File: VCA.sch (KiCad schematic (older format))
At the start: 27 parts, among them Q401 2N3904, Q402 2N3906, Q403 2N3904, U502 LM13700, U605 TL074

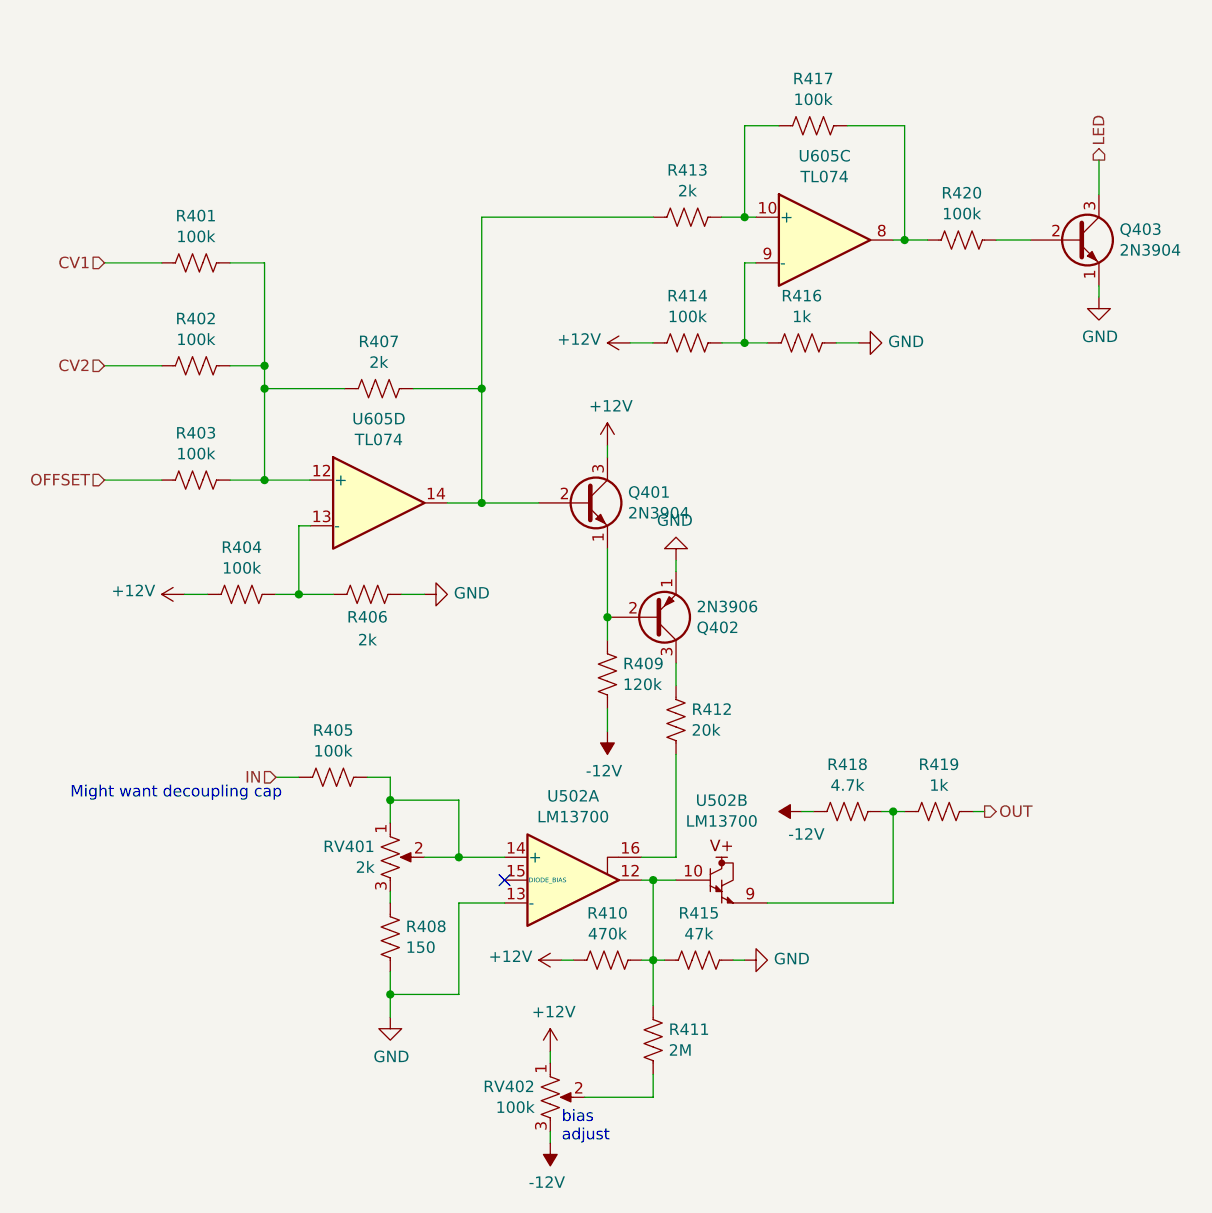
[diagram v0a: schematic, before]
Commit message: Began fixing backwards op amp issue
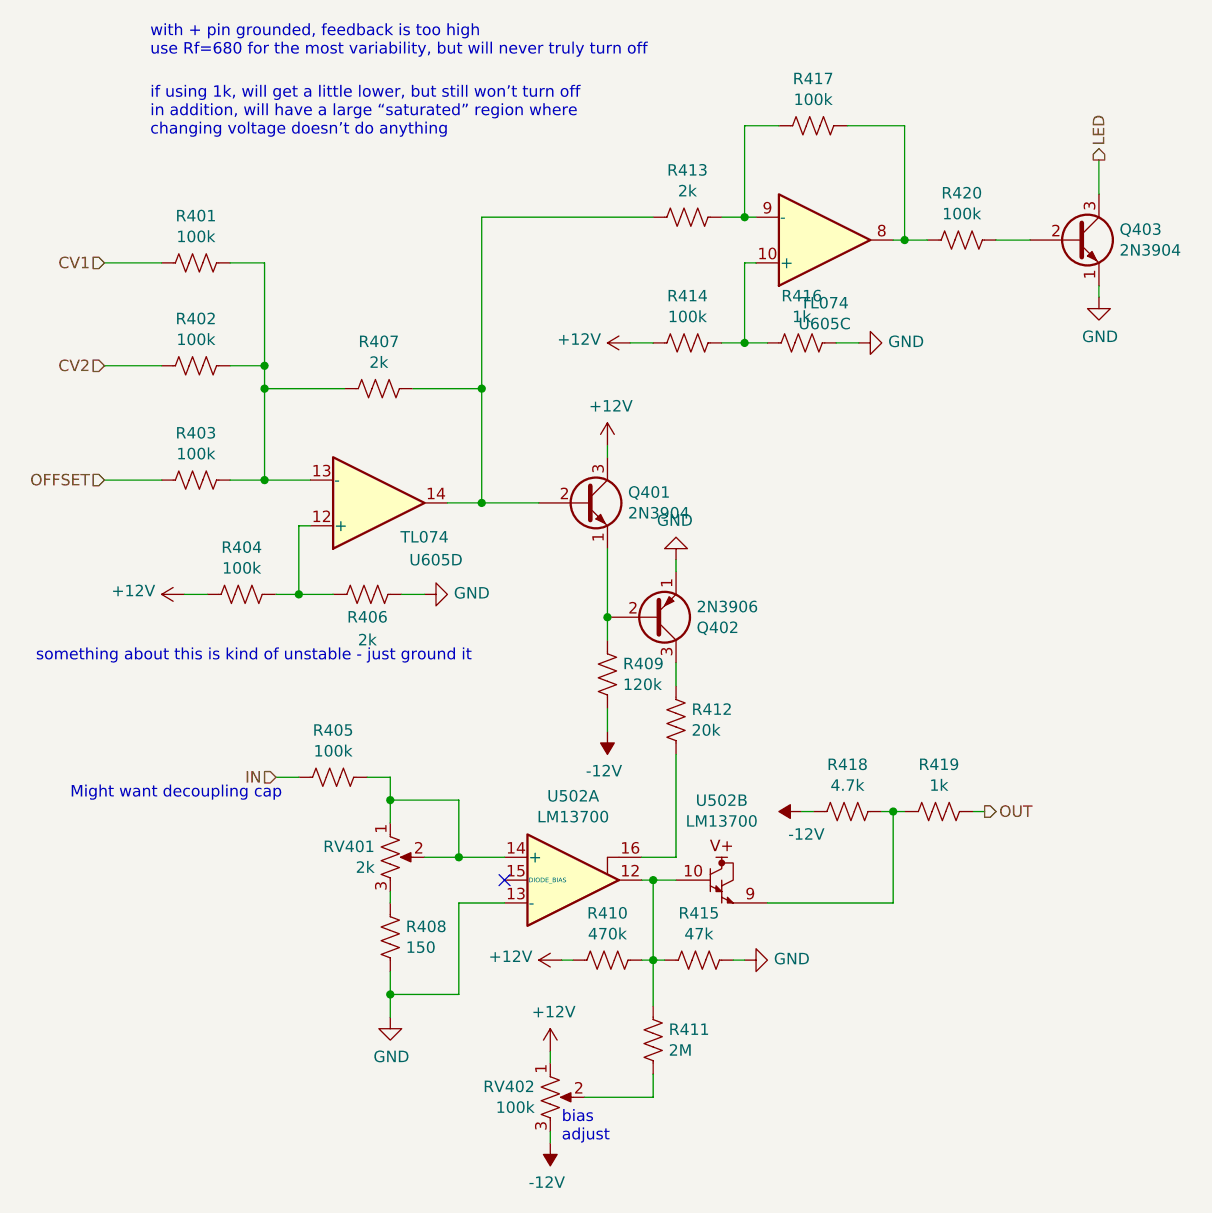
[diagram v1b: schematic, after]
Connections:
- net at R401.1, R402.1, R403.1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: now also U605.13 (-); no longer U605.12 (+)
- net at R404.1, R406.2: now also U605.12 (+); no longer U605.13 (-)
- net at R413.1, R417.2: now also U605.9 (-); no longer U605.10 (+)
- net at R414.1, R416.2: now also U605.10 (+); no longer U605.9 (-)
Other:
- note added: "if using 1k, will get a little lower, but still won’t turn off\nin addition, will have a large “saturated” region where \nchanging voltage doesn’t do anything"
- note added: "something about this is kind of unstable - just ground it"
- note added: "with + pin grounded, feedback is too high\nuse Rf=680 for the most variability, but will never truly turn off"
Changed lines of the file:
@@
 U 4 1 6035B5C1
 P 2400 3000
-F 0 "U605" H 2400 3367 50  0000 C CNN
-F 1 "TL074" H 2400 3276 50  0000 C CNN
+F 0 "U605" H 2650 3250 50  0000 C CNN
+F 1 "TL074" H 2600 3150 50  0000 C CNN
 F 2 "Package_DIP:DIP-14_W7.62mm" H 2400 3000 50  0001 C CNN
 F 3 "http://www.ti.com/lit/ds/symlink/tl081.pdf" H 2400 3000 50  0001 C CNN
 	4    2400 3000
-	1    0    0    -1
+	1    0    0    1
 $EndComp
 $Comp
@@
 F 3 "http://www.ti.com/lit/ds/symlink/tl081.pdf" H 4350 1850 50  0001 C CNN
 	3    4350 1850
-	1    0    0    -1
+	1    0    0    1
 $EndComp
 $Comp
@@
 Text Notes 3200 5800 0    50   ~ 0
 bias\nadjust
+Text Notes 900  3700 0    50   ~ 0
+something about this is kind of unstable - just ground it
+Text Notes 1400 1050 0    50   ~ 0
+with + pin grounded, feedback is too high\nuse Rf=680 for the most variability, but will never truly turn off
+Text Notes 1400 1400 0    50   ~ 0
+if using 1k, will get a little lower, but still won’t turn off\nin addition, will have a large “saturated” region where \nchanging voltage doesn’t do anything
 $EndSCHEMATC

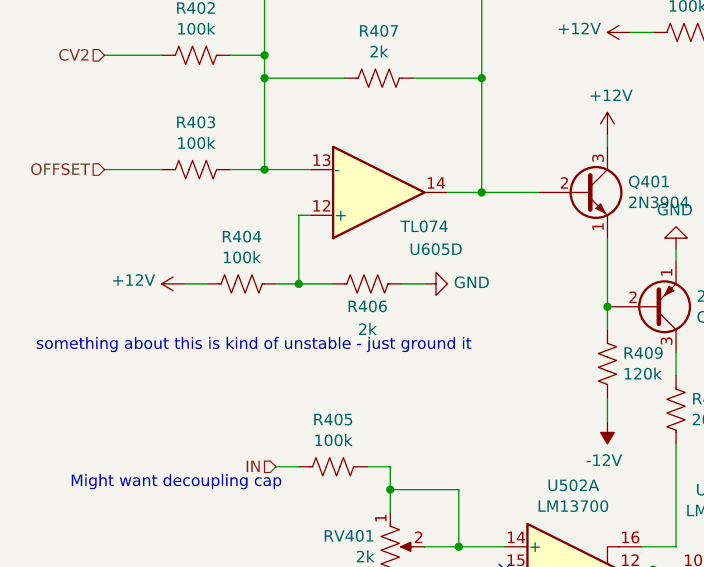
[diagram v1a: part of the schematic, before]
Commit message: Fixed op amp issue
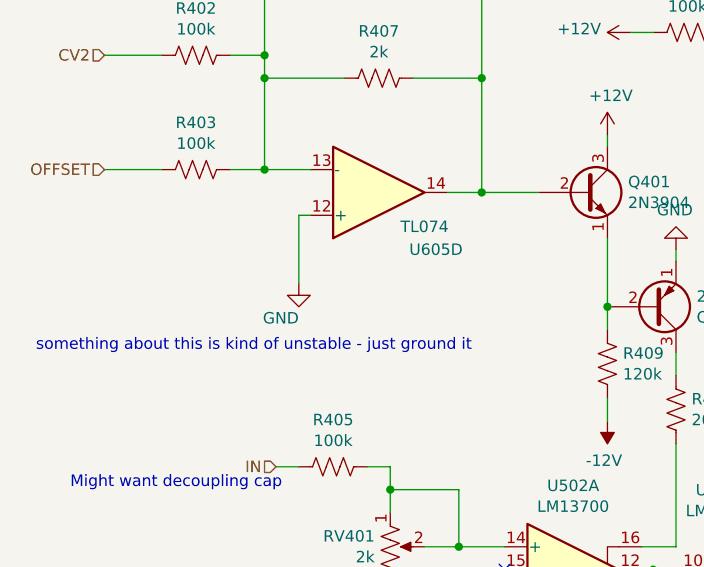
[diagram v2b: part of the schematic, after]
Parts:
- removed R404: 100k, Resistor_THT:R_Axial_DIN0207_L6.3mm_D2.5mm_P7.62mm_Horizontal, symbol Device:R_US
- removed R406: 2k, Resistor_THT:R_Axial_DIN0207_L6.3mm_D2.5mm_P7.62mm_Horizontal, symbol Device:R_US
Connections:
- net GND: now also U605.12 (+)
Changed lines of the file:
@@
-$EndComp
-$Comp
-L Device:R_US R406
-U 1 1 6036C3EB
-P 2350 3400
-F 0 "R406" V 2450 3400 50  0000 C CNN
-F 1 "2k" V 2550 3400 50  0000 C CNN
-F 2 "Resistor_THT:R_Axial_DIN0207_L6.3mm_D2.5mm_P7.62mm_Horizontal" V 2390 3390 50  0001 C CNN
-F 3 "~" H 2350 3400 50  0001 C CNN
-	1    2350 3400
-	0    1    1    0
 $EndComp
 $Comp
@@
 	0    1    1    0
 $EndComp
-$Comp
-L Device:R_US R404
-U 1 1 603714AC
-P 1800 3400
-F 0 "R404" V 1595 3400 50  0000 C CNN
-F 1 "100k" V 1686 3400 50  0000 C CNN
-F 2 "Resistor_THT:R_Axial_DIN0207_L6.3mm_D2.5mm_P7.62mm_Horizontal" V 1840 3390 50  0001 C CNN
-F 3 "~" H 1800 3400 50  0001 C CNN
-	1    1800 3400
-	0    1    1    0
-$EndComp
 Text HLabel 1200 1950 0    50   Input ~ 0
 CV1
@@
 	1900 2500 1900 2900
 Wire Wire Line
-	2200 3400 2050 3400
-Wire Wire Line
 	2100 3100 2050 3100
 Wire Wire Line
 	2050 3100 2050 3400
-Connection ~ 2050 3400
-Wire Wire Line
-	2050 3400 1950 3400
-Wire Wire Line
-	1550 3400 1650 3400
-Wire Wire Line
-	2600 3400 2500 3400
 $Comp
 L power:GND #PWR0403
 U 1 1 6038B60B
-P 2600 3400
-F 0 "#PWR0403" H 2600 3150 50  0001 C CNN
-F 1 "GND" V 2605 3272 50  0000 R CNN
-F 2 "" H 2600 3400 50  0001 C CNN
-F 3 "" H 2600 3400 50  0001 C CNN
-	1    2600 3400
-	0    -1   -1   0
-$EndComp
-$Comp
-L power:+12V #PWR0401
-U 1 1 6038C3CB
-P 1550 3400
-F 0 "#PWR0401" H 1550 3250 50  0001 C CNN
-F 1 "+12V" V 1565 3528 50  0000 L CNN
-F 2 "" H 1550 3400 50  0001 C CNN
-F 3 "" H 1550 3400 50  0001 C CNN
-	1    1550 3400
-	0    -1   -1   0
+P 2050 3400
+F 0 "#PWR0403" H 2050 3150 50  0001 C CNN
+F 1 "GND" H 2050 3250 50  0000 R CNN
+F 2 "" H 2050 3400 50  0001 C CNN
+F 3 "" H 2050 3400 50  0001 C CNN
+	1    2050 3400
+	1    0    0    -1
 $EndComp
 Wire Wire Line
